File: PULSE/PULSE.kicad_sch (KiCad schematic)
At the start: 0 parts

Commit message: all motors, drivers, steppers, and teensy added
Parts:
- added M1, M2, M3, M4, M5, M6, M7, M8: Motor_Servo, symbol Motor:Motor_Servo
- added STEP1, STEP2, STEP3: Stepper_Motor_Nema23, symbol Motor:Stepper_Motor_bipolar
- added U1: Teensy4.1, symbol teensy:Teensy4.1
- added U2: D1, symbol dm542t_digital_stepper_driver:DM542T_Digital_Stepper_Driver
- added U3: D2, symbol dm542t_digital_stepper_driver:DM542T_Digital_Stepper_Driver
- added U4: D3, symbol dm542t_digital_stepper_driver:DM542T_Digital_Stepper_Driver
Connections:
- new net Driver1DIR+: U1.33 (41_A17), U2.3 (DIR+)
- new net Driver1PUL+: U1.34 (GND), U2.1 (PUL+)
- new net Driver2DIR+: U1.35 (13_SCK_LED), U3.3 (DIR+)
- new net Driver2PUL+: U1.36 (14_A0_TX3_SPDIF_OUT), U3.1 (PUL+)
- new net Driver3DIR+: U1.37 (15_A1_RX3_SPDIF_IN), U4.3 (DIR+)
- new net Driver3PUL+: U1.38 (16_A2_RX4_SCL1), U4.1 (PUL+)
- new net STEP1A+: STEP1.1, U2.11 (A+)
- new net STEP1A-: STEP1.3, U2.12 (A-)
- new net STEP1B+: STEP1.2 (-), U2.13 (B+)
- new net STEP1B-: STEP1.4, U2.14 (B-)
- new net STEP2A+: STEP2.1, U3.11 (A+)
- new net STEP2A-: STEP2.3, U3.12 (A-)
- new net STEP2B+: STEP2.2 (-), U3.13 (B+)
- new net STEP2B-: STEP2.4, U3.14 (B-)
- new net STEP3A+: STEP3.1, U4.11 (A+)
- new net STEP3A-: STEP3.3, U4.12 (A-)
- new net STEP3B+: STEP3.2 (-), U4.13 (B+)
- new net STEP3B-: STEP3.4, U4.14 (B-)
- new net Servo1: M1.1 (PWM), U1.9 (7_RX2_OUT1A)
- new net Servo2: M2.1 (PWM), U1.6 (4_BCLK2)
- new net Servo3: M3.1 (PWM), U1.5 (3_LRCLK2)
- new net Servo4: M4.1 (PWM), U1.4 (2_OUT2)
- new net Servo5: M5.1 (PWM), U1.3 (1_TX1_CTX2_MISO1)
- new net Servo6: M6.1 (PWM), U1.2 (0_RX1_CRX2_CS1)

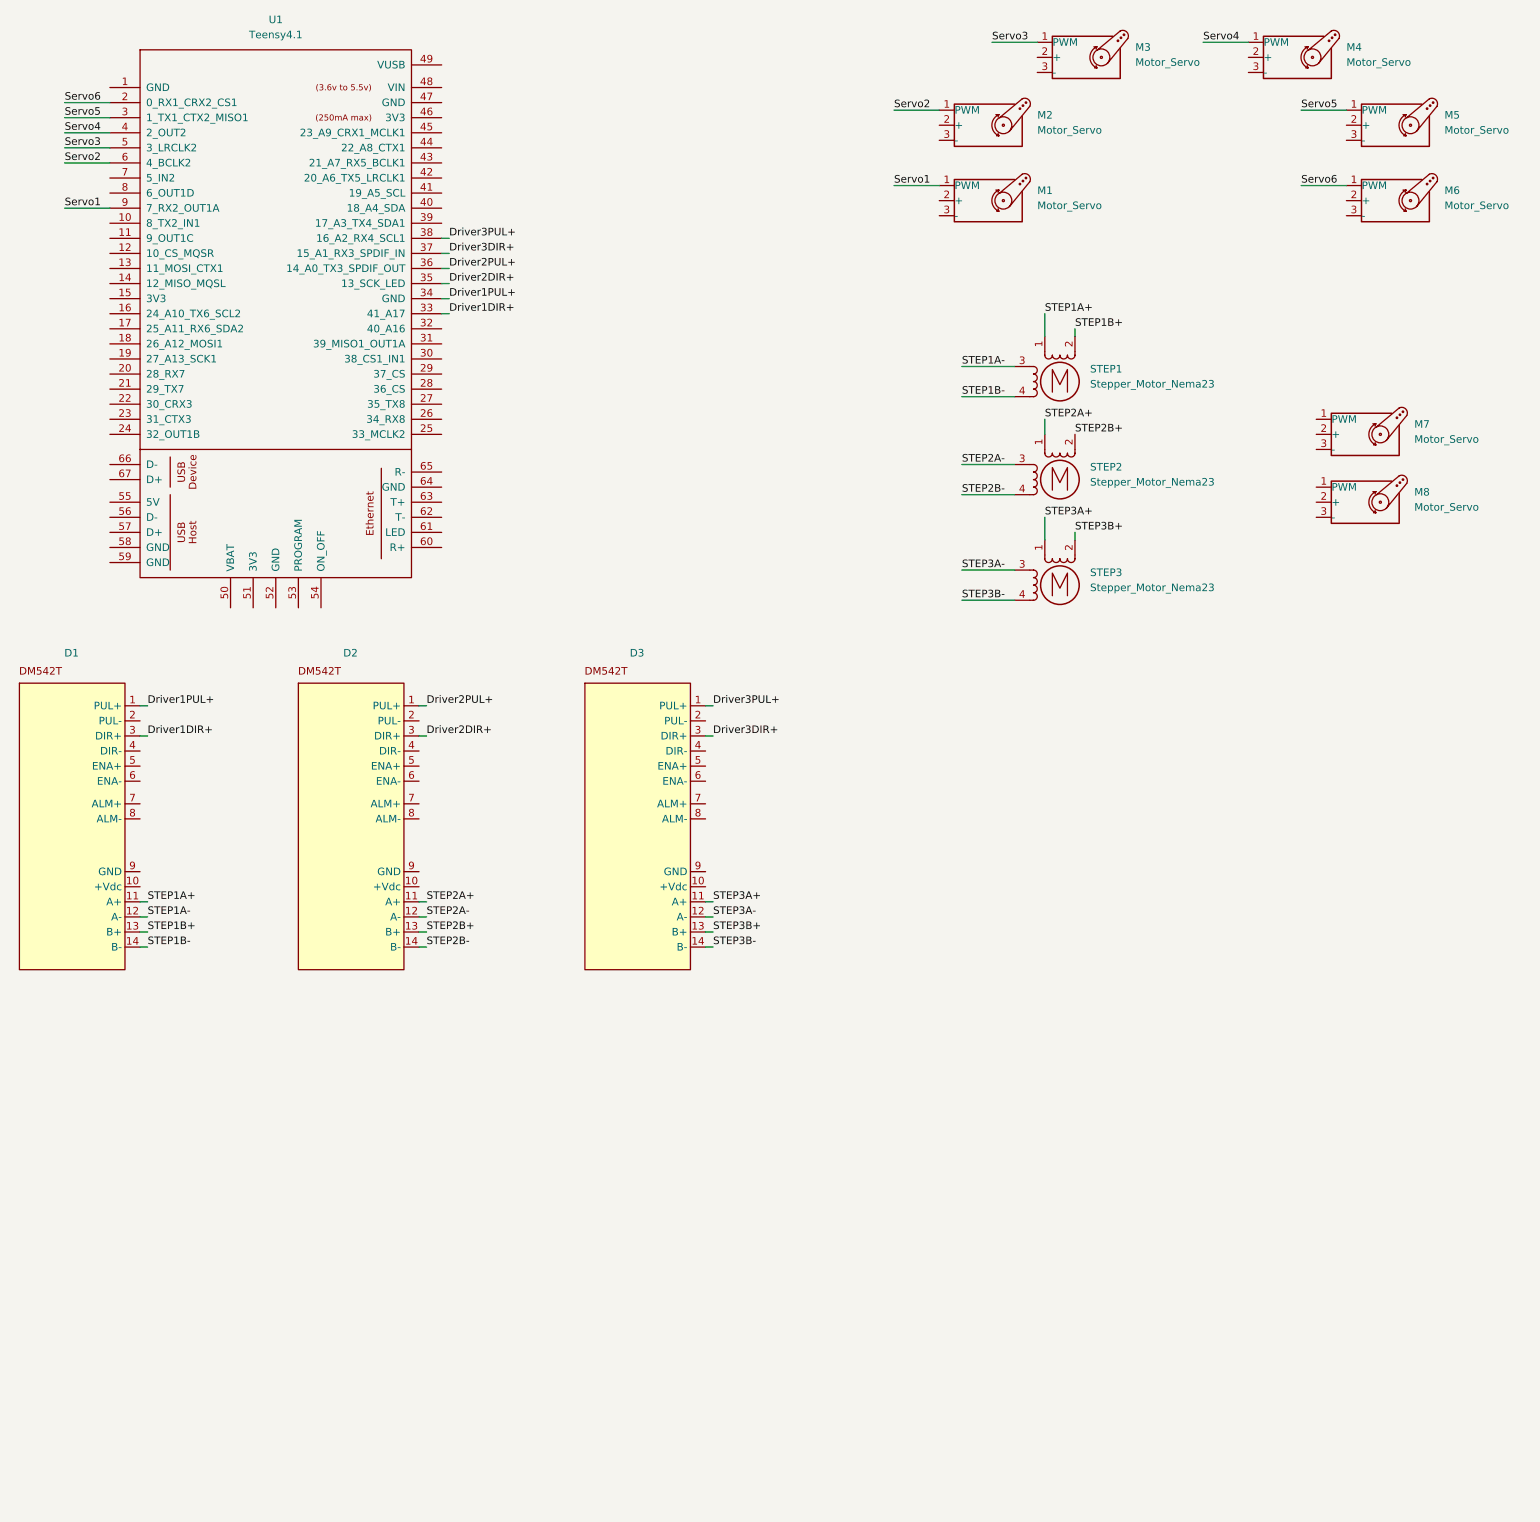
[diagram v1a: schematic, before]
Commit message: added gnds
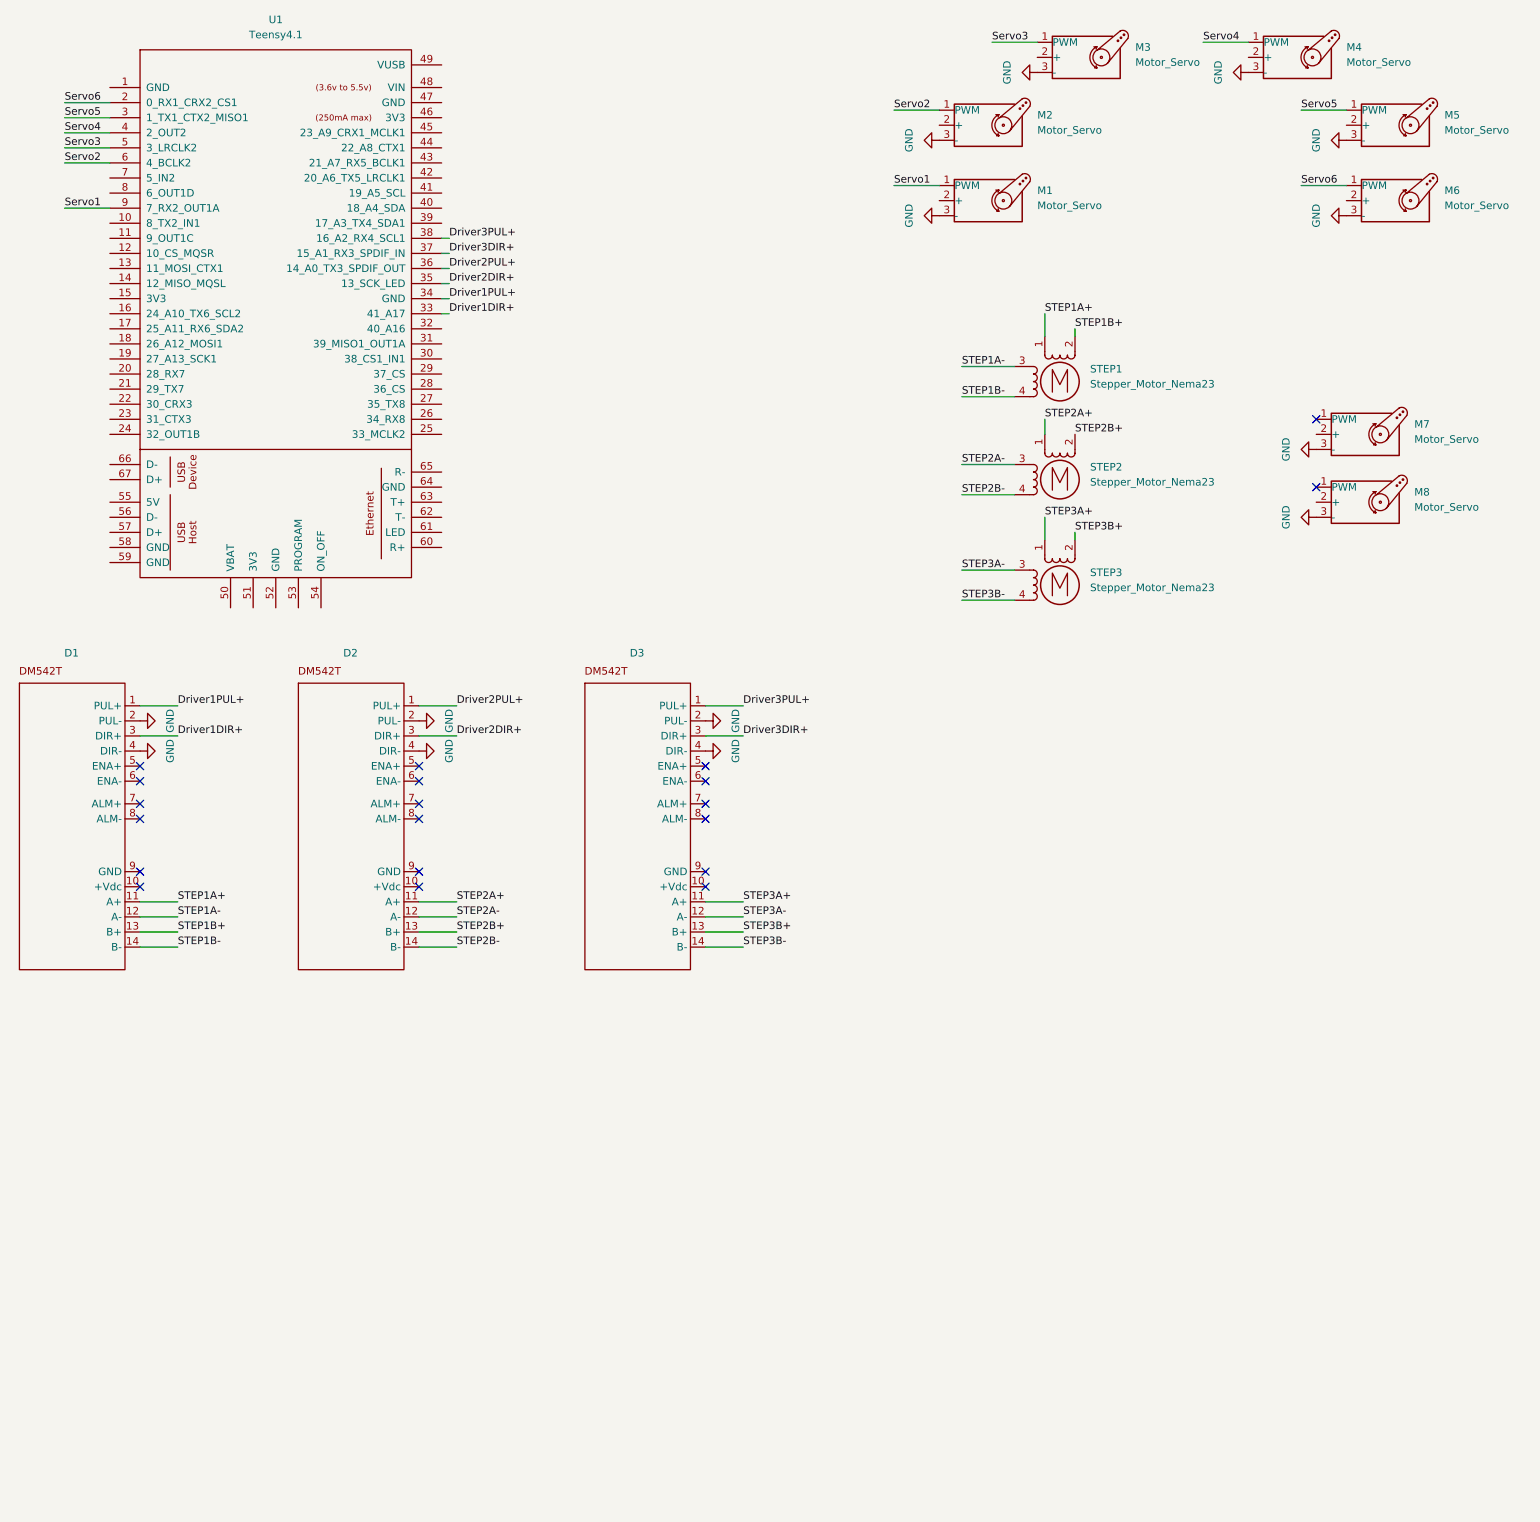
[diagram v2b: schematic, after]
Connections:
- net GND: now reaches M6.3 (-)
- net GND: now also M1.3 (-), M2.3 (-), M3.3 (-), M4.3 (-), M5.3 (-), M7.3 (-), M8.3 (-), U2.2 (PUL-), U2.4 (DIR-), U3.2 (PUL-), U3.4 (DIR-), U4.2 (PUL-), U4.4 (DIR-)
- no-connect marks 0 -> 20

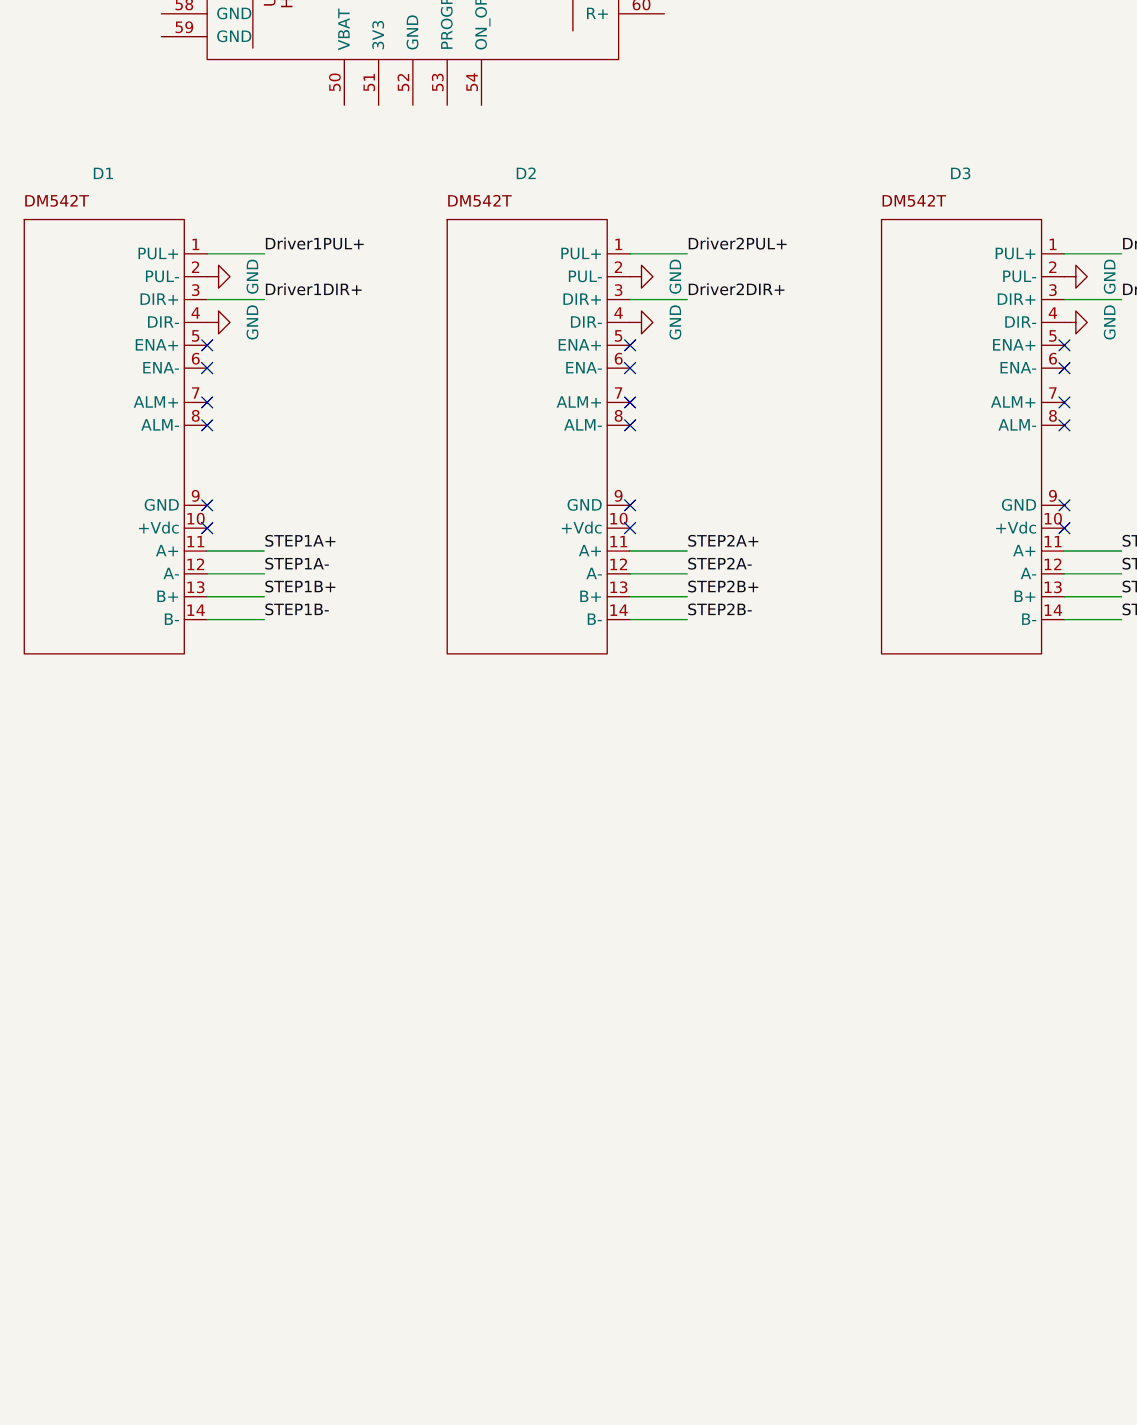
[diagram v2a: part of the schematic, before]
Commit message: added heatbed symols
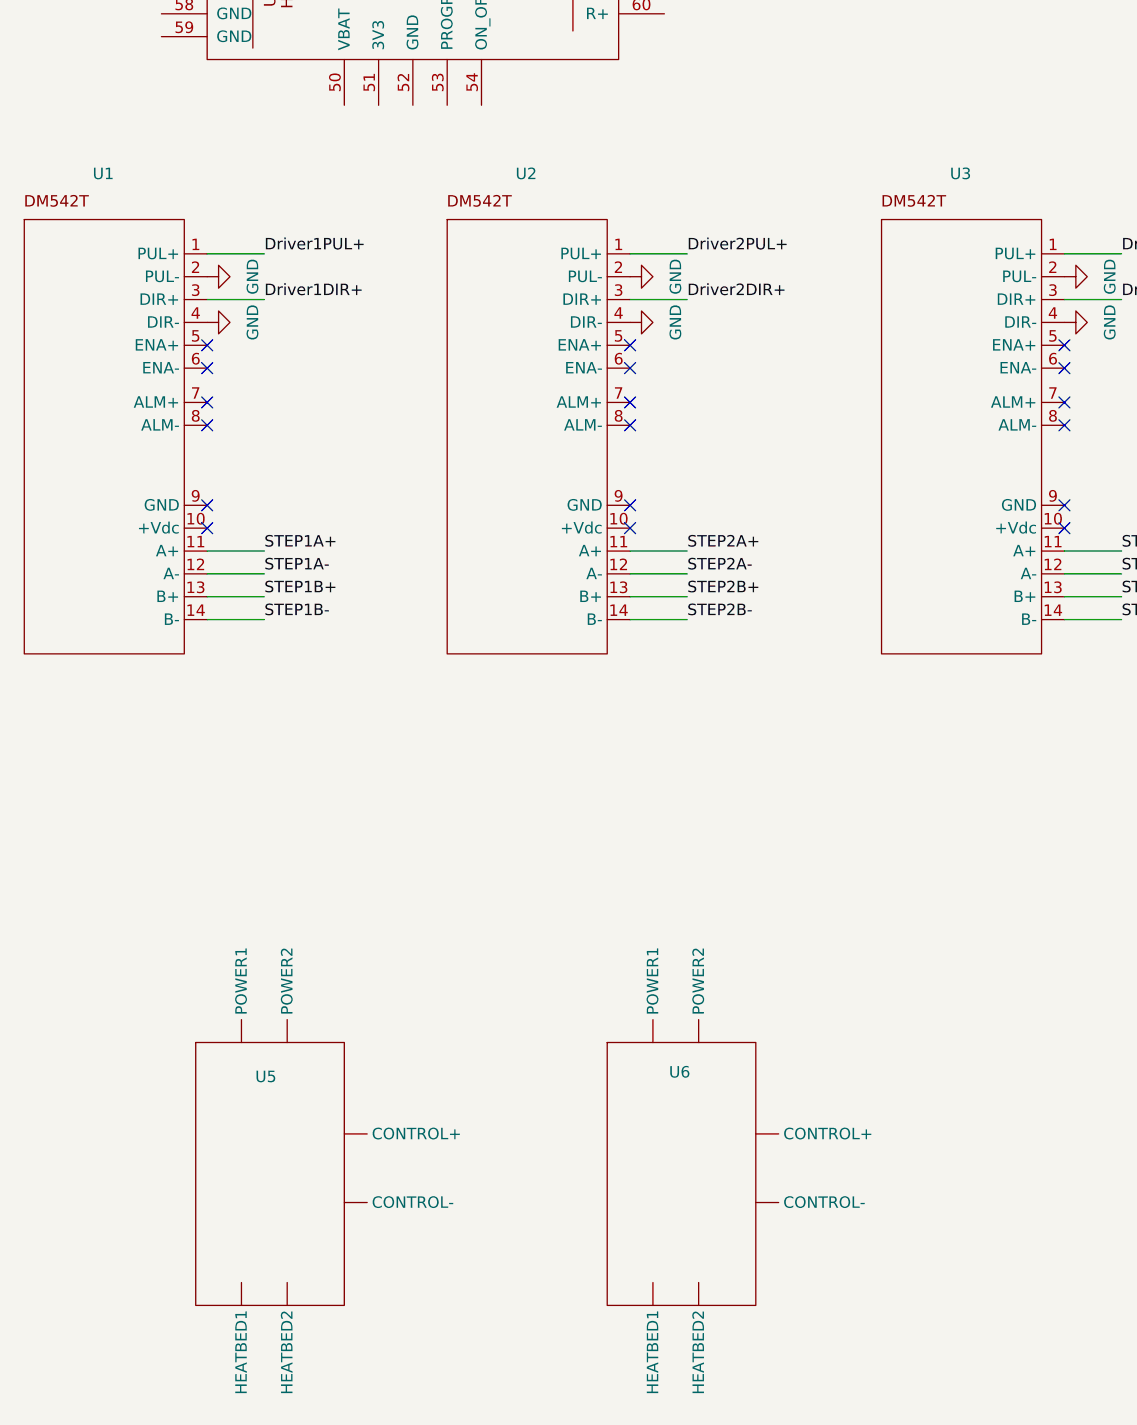
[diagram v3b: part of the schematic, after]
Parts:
- added U5, U6: ~, symbol lerdge_heatbed:lerdge_heatbed
- U2: value D1 -> U1
- U3: value D2 -> U2
- U4: value D3 -> U3
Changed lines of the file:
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@@
 	(generator "eeschema")
 	(generator_version "9.0")
-	(paper "A4")
+	(paper "A3")
 	(no_connect
 		(at 251.46 106.68)
@@
 	)
 	(symbol
+		(lib_id "lerdge_heatbed:lerdge_heatbed")
+		(at 59.69 228.6 0)
+		(unit 1)
+		(exclude_from_sim no)
+		(in_bom yes)
+		(on_board yes)
+		(dnp no)
+		(property "Reference" "U5"
+			(at 58.674 234.95 0)
+			(effects
+				(font
+					(size 1.27 1.27)
+				)
+				(justify left)
+			)
+		)
+		(property "Value" "~"
+			(at 72.39 245.7449 0)
+			(effects
+				(font
+					(size 1.27 1.27)
+				)
+				(justify left)
+			)
+		)
+		(property "Footprint" ""
+			(at 59.69 228.6 0)
+			(effects
+				(font
+					(size 1.27 1.27)
+				)
+				(hide yes)
+			)
+		)
+		(property "Datasheet" ""
+			(at 59.69 228.6 0)
+			(effects
+				(font
+					(size 1.27 1.27)
+				)
+				(hide yes)
+			)
+		)
+		(property "Description" ""
+			(at 59.69 228.6 0)
+			(effects
+				(font
+					(size 1.27 1.27)
+				)
+				(hide yes)
+			)
+		)
+		(pin ""
+		)
+		(pin ""
+		)
+		(pin ""
+		)
+		(pin ""
+		)
+		(pin ""
+		)
+		(pin ""
+		)
+		(instances
+			(project ""
+				(path "/2ccb6803-f597-4b91-b781-68e055fdefb5"
+					(reference "U5")
+					(unit 1)
+				)
+			)
+		)
+	)
+	(symbol
 		(lib_id "Motor:Motor_Servo")
 		(at 264.16 58.42 0)
@@
 			)
 		)
-		(property "Value" "D1"
+		(property "Value" "U1"
 			(at 41.803 134.62 0)
 			(effects
@@
 			)
 		)
-		(property "Value" "D2"
+		(property "Value" "U2"
 			(at 88.793 134.62 0)
 			(effects
@@
 			)
 		)
-		(property "Value" "D3"
+		(property "Value" "U3"
 			(at 137.053 134.62 0)
 			(effects
@@
 					(unit 1)
 				)
+			)
+		)
+	)
+	(symbol
+		(lib_name "lerdge_heatbed_1")
+		(lib_id "lerdge_heatbed:lerdge_heatbed")
+		(at 105.41 228.6 0)
+		(unit 1)
+		(exclude_from_sim no)
+		(in_bom yes)
+		(on_board yes)
+		(dnp no)
+		(property "Reference" "U6"
+			(at 104.648 234.442 0)
+			(effects
+				(font
+					(size 1.27 1.27)
+				)
+				(justify left)
+			)
+		)
+		(property "Value" "~"
+			(at 118.11 245.7449 0)
+			(effects
+				(font
+					(size 1.27 1.27)
+				)
+				(justify left)
+			)
+		)
+		(property "Footprint" ""
+			(at 105.41 228.6 0)
+			(effects
+				(font
+					(size 1.27 1.27)
+				)
+				(hide yes)
+			)
+		)
+		(property "Datasheet" ""
+			(at 105.41 228.6 0)
+			(effects
+				(font
+					(size 1.27 1.27)
+				)
+				(hide yes)
+			)
+		)
+		(property "Description" ""
+			(at 105.41 228.6 0)
+			(effects
+				(font
+					(size 1.27 1.27)
+				)
+				(hide yes)
+			)
+		)
+		(pin ""
+		)
+		(pin ""
+		)
+		(pin ""
+		)
+		(pin ""
+		)
+		(pin ""
+		)
+		(pin ""
+		)
+		(instances
+			(project "PULSE"
+				(path "/2ccb6803-f597-4b91-b781-68e055fdefb5"
+					(reference "U6")
+					(unit 1)
+				)
